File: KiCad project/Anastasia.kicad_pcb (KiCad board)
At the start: 4 copper layers, 32 x 33 mm, 95 parts, among them CON1 USB-MICRO-B, P1 LS013B4DN04, U1 EFM32GG332, U2 BQ25011, U3 BQ27421-G1, U4 IP4220CZ6, U5 MPU-9150, U6 AT24CM01, U7 AFE4403, U8 nRF8001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

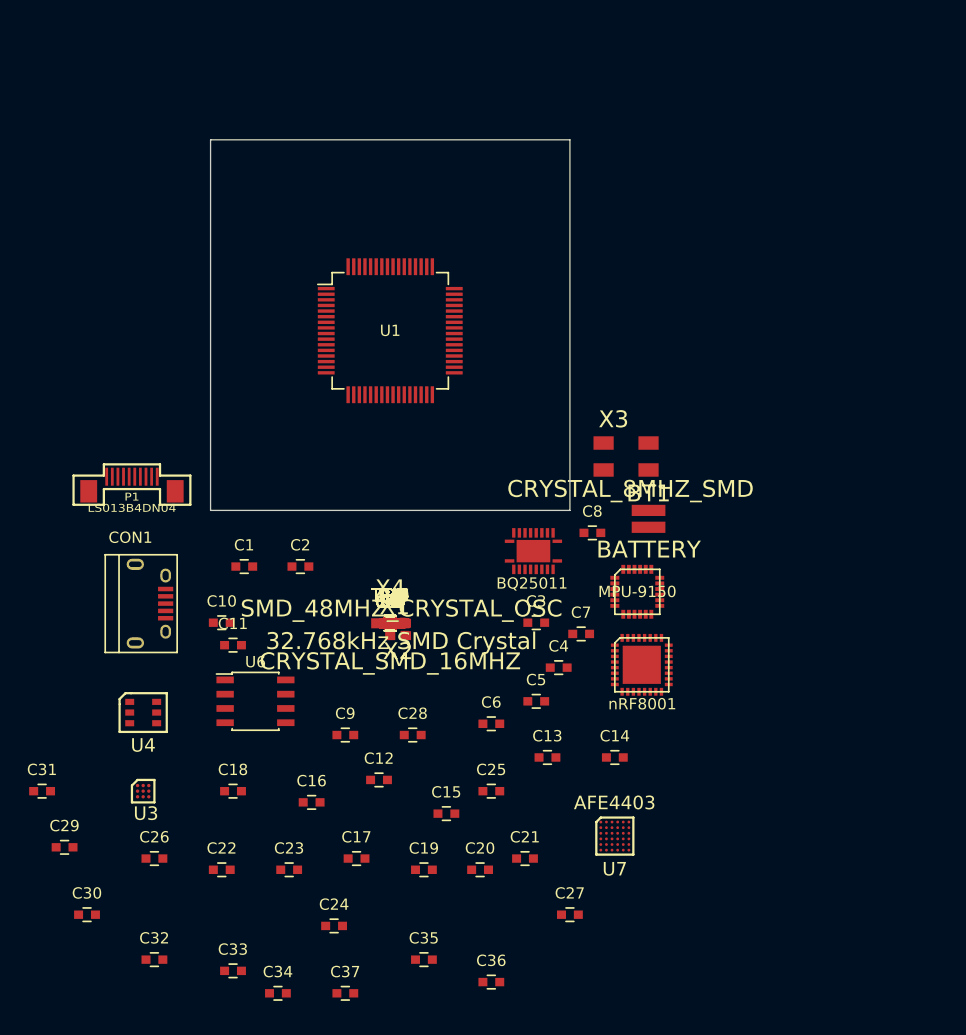
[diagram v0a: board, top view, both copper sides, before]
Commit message: Schematics, PCB design
New schematics for the pulse oximeter, PCB layout design
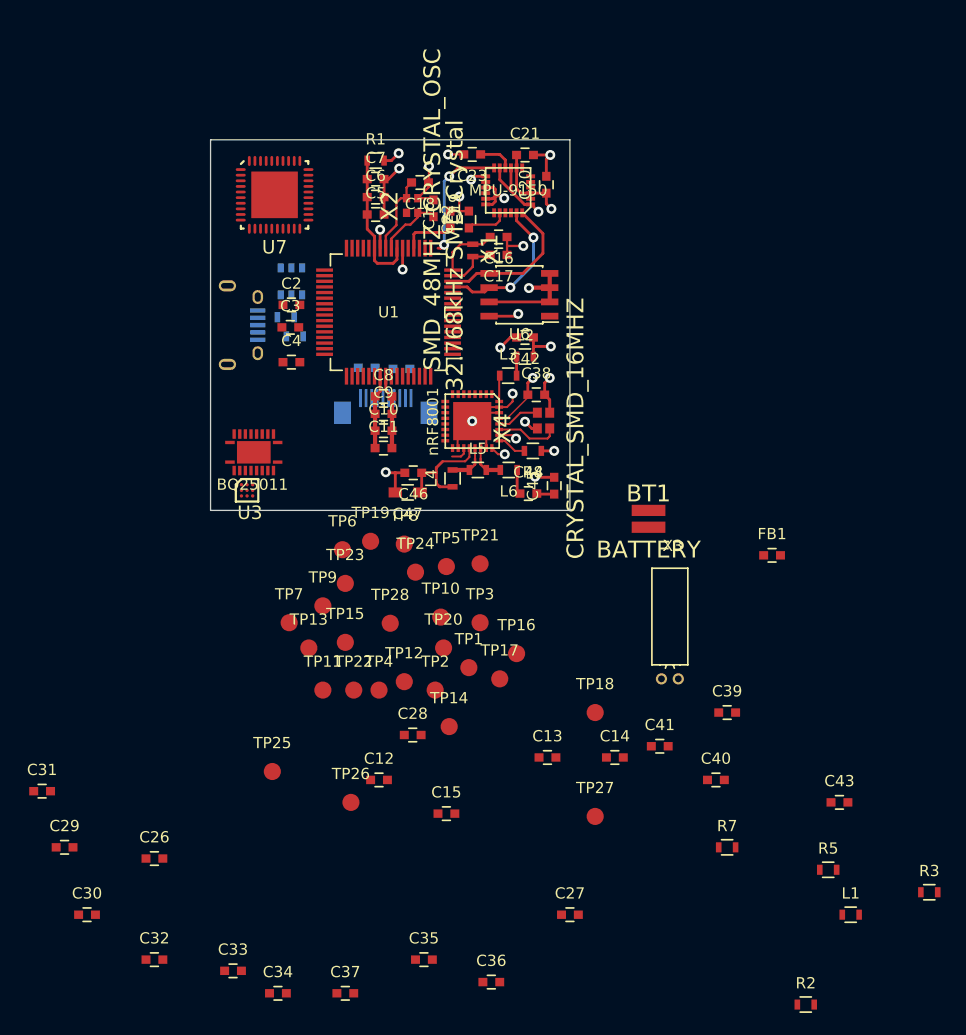
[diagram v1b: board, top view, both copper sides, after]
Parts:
- added TP19: TESTPAD, Measurement_Points:Measurement_Point_Round-SMD-Pad_Small, F.Cu at (84.2, 55.8)
- added TP20: TESTPAD, Measurement_Points:Measurement_Point_Round-SMD-Pad_Small, F.Cu at (90.8, 65.2)
- added TP21: TESTPAD, Measurement_Points:Measurement_Point_Round-SMD-Pad_Small, F.Cu at (94.0, 57.8)
- added TP22: TESTPAD, Measurement_Points:Measurement_Point_Round-SMD-Pad_Small, F.Cu at (82.8, 69.0)
- added TP23: TESTPAD, Measurement_Points:Measurement_Point_Round-SMD-Pad_Small, F.Cu at (82.0, 59.5)
- added TP24: TESTPAD, Measurement_Points:Measurement_Point_Round-SMD-Pad_Small, F.Cu at (88.2, 58.5)
- added TP25: TESTPAD, Measurement_Points:Measurement_Point_Round-SMD-Pad_Small, F.Cu at (75.5, 76.2)
- added TP26: TESTPAD, Measurement_Points:Measurement_Point_Round-SMD-Pad_Small, F.Cu at (82.5, 79.0)
- added TP27: TESTPAD, Measurement_Points:Measurement_Point_Round-SMD-Pad_Small, F.Cu at (104.2, 80.2)
- added TP28: TESTPAD, Measurement_Points:Measurement_Point_Round-SMD-Pad_Small, F.Cu at (86.0, 63.1)
- C24, C25, CON1, P1, R4, R6, U4: moved to B.Cu
- U7: value AFE4403 -> AFE4490; footprint Anastasia:DSBGA36 -> Anastasia:QFN40
- X3: value CRYSTAL_8MHZ_SMD -> CRYSTAL; footprint Anastasia:5x3.2_Crystal_SMD -> Crystals:Crystal_Round_Horizontal_3mm
- moved C23 65.8 mm to (93.3, 21.3), turned to 180 degrees
- moved U7 64.6 mm to (75.7, 24.9)
- moved C21 62.6 mm to (98.0, 21.4)
- moved C22 61.9 mm to (93.0, 27.1), turned to 90 degrees
- moved C20 61.3 mm to (99.9, 24.0), turned to 90 degrees
- moved C19 58.9 mm to (89.8, 26.1), turned to 270 degrees
- moved C18 56.7 mm to (88.7, 23.8), turned to 180 degrees
- moved C17 55.2 mm to (95.7, 30.2), turned to 180 degrees
- moved R3 53.6 mm to (134.0, 87.0)
- moved C16 53.0 mm to (95.7, 28.6), turned to 180 degrees
- moved R2 50.2 mm to (123.0, 97.0)
- moved C24 50.0 mm to (87.0, 40.4)
- moved L1 48.5 mm to (127.0, 89.0)
- moved C6 48.0 mm to (84.7, 25.1)
- moved C5 45.6 mm to (84.7, 26.6)
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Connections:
- C46 pad 2: Net-(C46-Pad2) -> GND
- C47 pad 1: Net-(C47-Pad1) -> Net-(C46-Pad1)
- C47 pad 2: Net-(C46-Pad2) -> GND
- L4 pad 1: Net-(L4-Pad1) -> Net-(C46-Pad1)
- U1 pad 17: Net-(U1-Pad17) -> /IMU/IMU_INT
- U8 pad 20: Net-(L4-Pad1) -> Net-(C46-Pad1)
- X1 pad 1: Net-(X1-Pad1) -> Net-(C16-Pad2)
- X3 pad 1: Net-(C34-Pad1) -> Net-(C35-Pad1)
- X3 pad 2: Net-(C35-Pad1) -> Net-(C34-Pad1)
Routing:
- net GND: track 0.00 -> 80.3 mm, vias 0 -> 18
- net +3V3: track 0.00 -> 32.9 mm, vias 0 -> 9
- net /uC part B/I2C1_SDA: track 0.00 -> 13.6 mm, vias 0 -> 2
- net /uC part B/I2C1_SCL: track 0.00 -> 13.5 mm
- net Net-(C5-Pad1): track 0.00 -> 12.4 mm
- net /IMU/IMU_INT: track 0.00 -> 11.3 mm, vias 0 -> 2
- net Net-(C46-Pad1): track 0.00 -> 10.5 mm
- net Net-(C18-Pad2): track 0.00 -> 7.10 mm
- net Net-(C19-Pad2): track 0.00 -> 5.93 mm
- net Net-(C39-Pad1): track 0.00 -> 5.61 mm
- net Net-(C16-Pad2): track 0.00 -> 5.51 mm
- net /Power/MCU_RESET: track 0.00 -> 4.80 mm
- net Net-(C17-Pad2): track 0.00 -> 4.64 mm
- net Net-(C40-Pad1): track 0.00 -> 3.81 mm
- net Net-(C22-Pad1): track 0.00 -> 3.72 mm
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- added copper zone on In2.Cu, net +3V3
- added copper zone on In1.Cu, net GND
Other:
- net class Default: clearance 0.254 -> 0.127
- rule trace_clearance: 0.254 -> 0.127

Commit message: PCB design
Routing for the main components, except for the power section
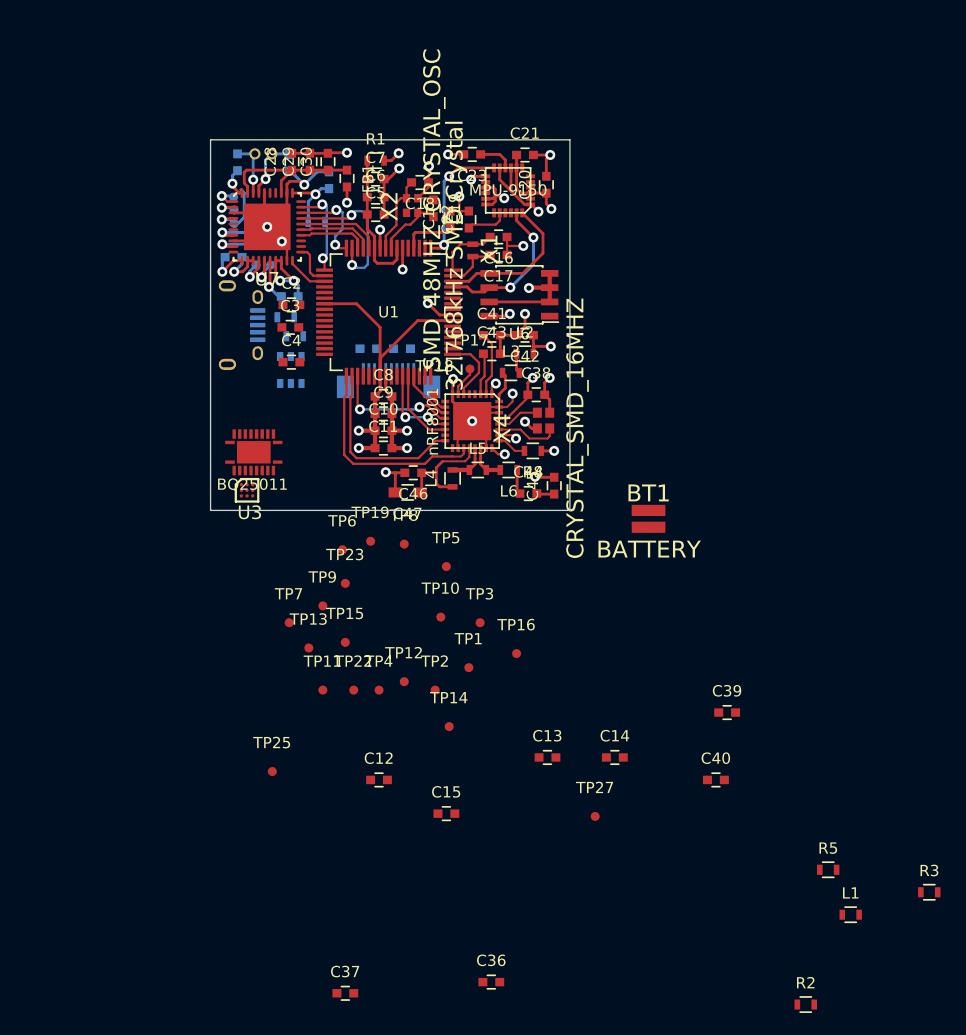
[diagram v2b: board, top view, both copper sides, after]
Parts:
- C26, C27, C31, C32, C33, C34, C35, R7, X3: moved to B.Cu
- TP1, TP10, TP11, TP12, TP13, TP14, TP15, TP16, TP17, TP18, TP19, TP2, TP22, TP23, TP25, TP27, TP3, TP4, TP5, TP6, TP7, TP8, TP9: footprint Measurement_Points:Measurement_Point_Round-SMD-Pad_Small -> Anastasia:Test_Point_Round-SMD-Pad
- TP20, TP21, TP24, TP26, TP28: footprint Measurement_Points:Measurement_Point_Round-SMD-Pad_Small -> Anastasia:Test_Point_Round-SMD-Pad; moved to B.Cu
- moved C34 74.1 mm to (72.4, 22.0), turned to 270 degrees
- moved C35 72.0 mm to (77.0, 22.1), turned to 270 degrees
- moved C30 70.4 mm to (80.5, 21.9), turned to 90 degrees
- moved C27 67.9 mm to (75.7, 26.4)
- moved R7 66.6 mm to (79.5, 27.3)
- moved C33 65.1 mm to (74.2, 28.9)
- moved C29 64.8 mm to (78.8, 21.9), turned to 90 degrees
- moved C32 62.9 mm to (72.0, 30.4)
- moved C31 60.1 mm to (80.5, 23.6), turned to 90 degrees
- moved X3 59.1 mm to (74.7, 21.2)
- moved C28 52.2 mm to (77.2, 21.9), turned to 90 degrees
- moved C26 51.5 mm to (77.0, 34.0), turned to 180 degrees
- moved FB1 50.6 mm to (82.2, 23.4), turned to 270 degrees
- moved C43 50.5 mm to (95.0, 39.0)
- moved TP26 48.6 mm to (74.0, 31.1)
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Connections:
- C29 pad 1: Net-(C29-Pad1) -> Net-(C28-Pad1)
- C30 pad 1: Net-(C30-Pad1) -> Net-(C28-Pad1)
- FB1 pad 1: Net-(C30-Pad1) -> Net-(C28-Pad1)
- R7 pad 2: /Pulse oximeter /RESET -> /uC part B/PD5
- U1 pad 1: Net-(U1-Pad1) -> /Bluetooth LE/ACTIVE
- U1 pad 32: /uC part B/PD4 -> /Pulse oximeter /ADC_RDY
- U1 pad 34: /Power/GAUGE_SDA -> /Pulse oximeter /DIAG_END
- U1 pad 35: /Power/GAUGE_SCL -> /Pulse oximeter /AFE_PDN
- U1 pad 37: /uC part B/PC6 -> /Power/GAUGE_SDA
- U1 pad 38: Net-(U1-Pad38) -> /Power/GAUGE_SCL
- U1 pad 51: Net-(U1-Pad51) -> /uC part C/PF2
- U7 pad 13: Net-(U7-Pad13) -> GND
- U7 pad 29: /Pulse oximeter /RESET -> /uC part B/PD5
- U7 pad 33: Net-(C30-Pad1) -> Net-(C28-Pad1)
- U7 pad 39: Net-(C30-Pad1) -> Net-(C28-Pad1)
- U8 pad 12: /Bluetooth LE/REQN -> /uC part C/PF2
- U8 pad 16: /Bluetooth LE/RDYN -> /uC part C/PF1
- U8 pad 19: /Bluetooth LE/RESET_RADIO -> /uC part C/PF0
- X3 pad 1: Net-(C35-Pad1) -> Net-(C34-Pad1)
- X3 pad 2: Net-(C34-Pad1) -> Net-(C35-Pad1)
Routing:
- net GND: track 80.3 -> 139.6 mm, vias 18 -> 29
- net +3V3: track 32.9 -> 74.3 mm, vias 9 -> 17
- net /uC part C/PF0: track 0.00 -> 19.0 mm
- net /uC part C/PF1: track 0.00 -> 16.1 mm
- net /Pulse oximeter /SPIEN: track 0.00 -> 13.8 mm, vias 0 -> 2
- net Net-(C28-Pad1): track 0.00 -> 13.6 mm
- net /uC part C/PF2: track 0.00 -> 11.3 mm, vias 0 -> 2
- net /uC part B/PD5: track 0.00 -> 8.39 mm, vias 0 -> 2
- net /Pulse oximeter /ADC_RDY: track 0.00 -> 8.16 mm, vias 0 -> 2
- net /Display/DISP_SI: track 0.00 -> 7.55 mm, vias 0 -> 2
- net /Pulse oximeter /MOSI: track 0.00 -> 7.51 mm
- net /Bluetooth LE/MISO: track 0.00 -> 6.97 mm
- net /Pulse oximeter /MISO: track 0.00 -> 6.90 mm
- net /Pulse oximeter /SCLK: track 0.00 -> 6.10 mm
- net Net-(TP20-Pad1): track 0.00 -> 6.02 mm, vias 0 -> 1
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
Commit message: PCB finalised, Gerbers created for v0.5
New footprints, fixes in schematic, PCB final design, plotted Gerbers
for prototype production
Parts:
- removed TP1, TP10, TP12, TP13, TP14, TP15, TP16, TP2, TP3, TP4, TP5, TP6, TP8, TP9: TESTPAD, Anastasia:Test_Point_Round-SMD-Pad
- added D1: PHOTODIODE, Anastasia:BPW34S, F.Cu at (108.1, 47.9)
- added D2: RED_LED, Resistors_SMD:R_0603_HandSoldering, F.Cu at (108.2, 44.7)
- added D3: IR_LED, Anastasia:2x1.25mm_LED, F.Cu at (108.2, 43.0)
- added REF**: Symbol_OSHW-Logo_SilkScreen, Symbols:Symbol_OSHW-Logo_SilkScreen, B.Cu at (93.3, 46.7)
- added SW1: SWITCH, Anastasia:KMS_SMD_SW, B.Cu at (99.8, 25.0)
- added SW2: SWITCH, Anastasia:KMS_SMD_SW, B.Cu at (99.7, 32.2)
- added SW3: SWITCH, Anastasia:KMS_SMD_SW, B.Cu at (99.7, 37.7)
- added SW4: SWITCH, Anastasia:KMS_SMD_SW, B.Cu at (99.7, 49.4)
- BT1, C14, C36, C37, C39, C40: moved to B.Cu
- R3: value 1K6 -> 4K7
- moved R2 71.6 mm to (75.7, 43.2)
- moved L1 68.1 mm to (72.8, 47.8)
- moved R3 67.1 mm to (80.7, 46.2), turned to 270 degrees
- moved R5 57.6 mm to (78.8, 50.5)
- moved C37 57.3 mm to (92.8, 39.8)
- moved C36 53.6 mm to (93.5, 41.4), turned to 180 degrees
- moved C13 47.3 mm to (71.5, 37.2), turned to 90 degrees
- moved TP25 46.9 mm to (107.0, 41.5)
- moved TP11 44.2 mm to (97.8, 28.6)
- moved C14 40.8 mm to (76.2, 47.2), turned to 90 degrees
- moved TP27 39.1 mm to (109.5, 41.5)
- moved C40 37.9 mm to (99.0, 42.6)
- moved BT1 36.7 mm to (72.7, 47.8)
- moved C15 34.7 mm to (73.0, 50.3), turned to 180 degrees
- moved C12 33.9 mm to (72.8, 45.4)
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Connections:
- TP11 pad 1: /uC part B/I2C1_SDA -> /uC part B/I2C1_SCL
- U1 pad 12: /uC part B/PC3 -> Net-(SW2-Pad1)
- U1 pad 18: Net-(U1-Pad18) -> /uC part A/PA9
- U1 pad 19: Net-(U1-Pad19) -> /uC part A/PA10
- U1 pad 2: Net-(U1-Pad2) -> /Power/ISET
- U1 pad 3: Net-(U1-Pad3) -> /Power/CE
- U1 pad 36: /uC part B/PD8 -> /Power/GPOUT
- U1 pad 57: Net-(U1-Pad57) -> /Display/DISP_ON/OFF
- U1 pad 58: Net-(U1-Pad58) -> /Display/DISP_CS
- U2 pad 13: /Power/PG -> /Power/ISET
- U2 pad 14: (no net) -> /Power/PG
- U2 pad 7: /Power/STAT1 -> /uC part A/PA9
- U2 pad 8: /Power/STAT2 -> /uC part A/PA10
- U4 pad 4: Net-(CON1-Pad3) -> Net-(CON1-Pad2)
- U4 pad 6: Net-(CON1-Pad2) -> Net-(CON1-Pad3)
- U5 pad 23: /uC part B/I2C1_SDA -> /uC part B/I2C1_SCL
- U5 pad 24: /uC part B/I2C1_SCL -> /uC part B/I2C1_SDA
- U6 pad 5: /uC part B/I2C1_SCL -> /uC part B/I2C1_SDA
- U6 pad 6: /uC part B/I2C1_SDA -> /uC part B/I2C1_SCL
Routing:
- net GND: track 139.6 -> 203.0 mm, vias 29 -> 43
- net +3V3: track 74.3 -> 102.0 mm, vias 17 -> 21
- net Net-(TP23-Pad1): track 0.00 -> 27.5 mm
- net /Power/GPOUT: track 0.00 -> 27.4 mm, vias 0 -> 3
- net /Power/CE: track 0.00 -> 27.2 mm, vias 0 -> 4
- net /Power/GAUGE_SDA: track 0.00 -> 26.2 mm, vias 0 -> 3
- net /Power/GAUGE_SCL: track 0.00 -> 25.6 mm, vias 0 -> 3
- net /Power/ISET: track 0.00 -> 25.0 mm, vias 0 -> 4
- net /uC part A/PA10: track 0.00 -> 24.1 mm, vias 0 -> 2
- net /uC part A/PA9: track 0.00 -> 23.4 mm, vias 0 -> 2
- net USB_VBUS: track 0.00 -> 22.9 mm, vias 0 -> 2
- net Net-(SW1-Pad3): track 0.00 -> 17.7 mm, vias 0 -> 1
- net Net-(SW4-Pad3): track 0.00 -> 17.0 mm, vias 0 -> 1
- net Net-(SW2-Pad1): track 0.00 -> 15.5 mm, vias 0 -> 1
- net Net-(BT1-Pad1): track 0.00 -> 11.1 mm, vias 0 -> 1
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- added copper zone on In1.Cu, net (none)
- added copper zone on B.Cu, net USB_VBUS
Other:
- board size 32 x 33 mm -> 44 x 33 mm
- board text added: "Apr 2015"
- board text added: "N"
- board text added: "P"
- board text added: "RF"
- board text added: "SENSOR"
- board text added: "SMARTWATCH"
- board text added: "V"
- board text added: "V0.5"
- board text added: "sumanguru"

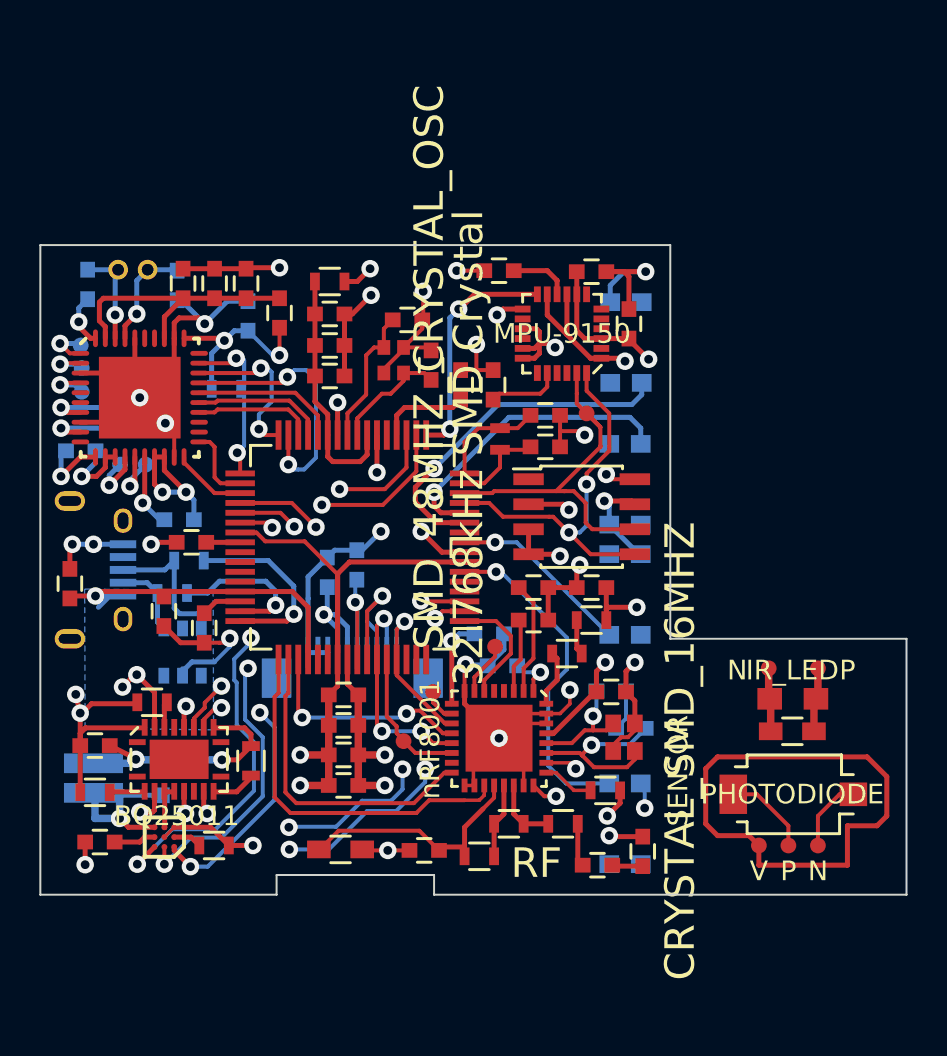
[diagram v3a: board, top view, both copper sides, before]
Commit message: Refactoring and assembly assist files
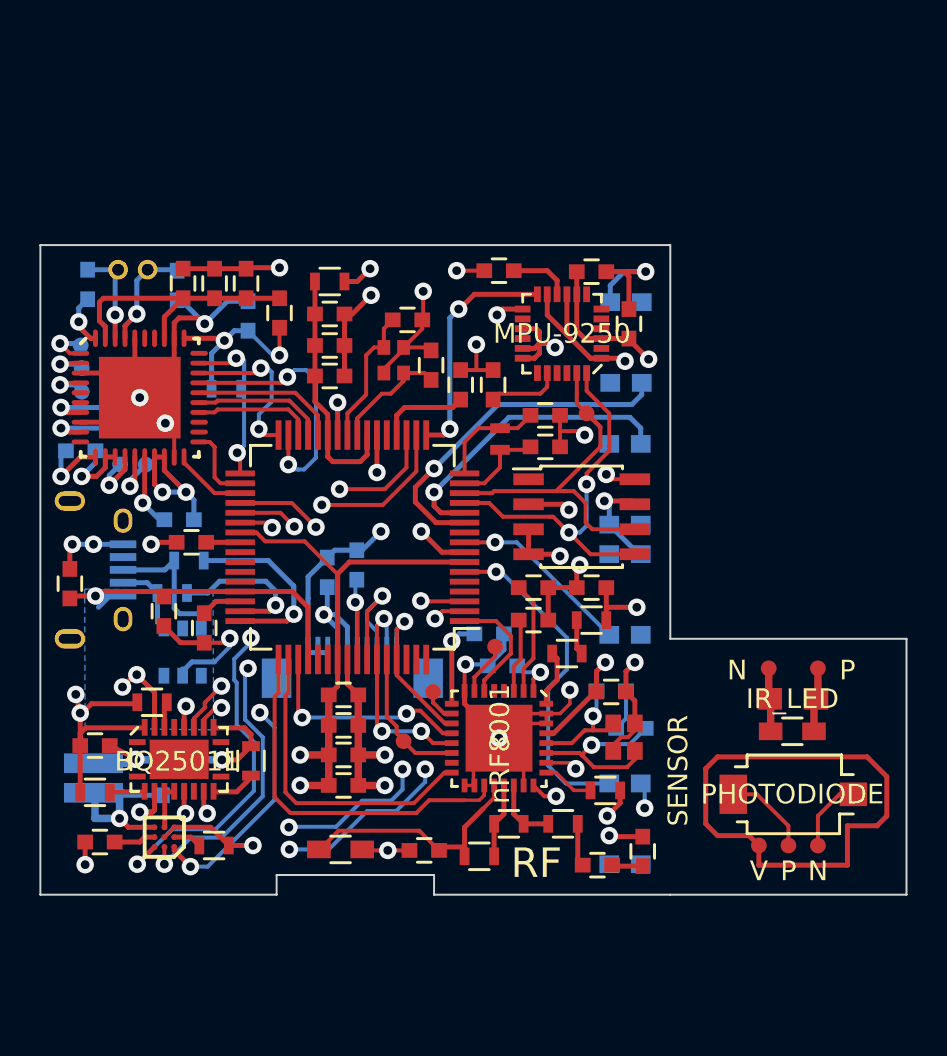
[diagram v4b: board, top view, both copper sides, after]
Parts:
- C13, C20, C23, C24, C30, C31, C32: value 0.1U -> 100N
- C16, C17: value C -> 15P
- C18, C19: value C -> 9P
- C34, C35: value C -> 10P
- FB1: value FILTER -> FB1
- U5: value MPU-9150 -> MPU-9250
- U6: value AT24CM01 -> AT24C256
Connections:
- U5 pad 5: Net-(U5-Pad5) -> GND
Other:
- board text added: "16M"
- board text added: "32K"
- board text added: "48M"

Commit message: Modifications for compliance with CERN OHL
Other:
- board text added: "LICENSED UNDER CERN OHL v1.2"
